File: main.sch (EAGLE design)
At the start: 9 parts, among them IC1 7805TV, IC3 LP298XS, U1 6SLX9TQG144

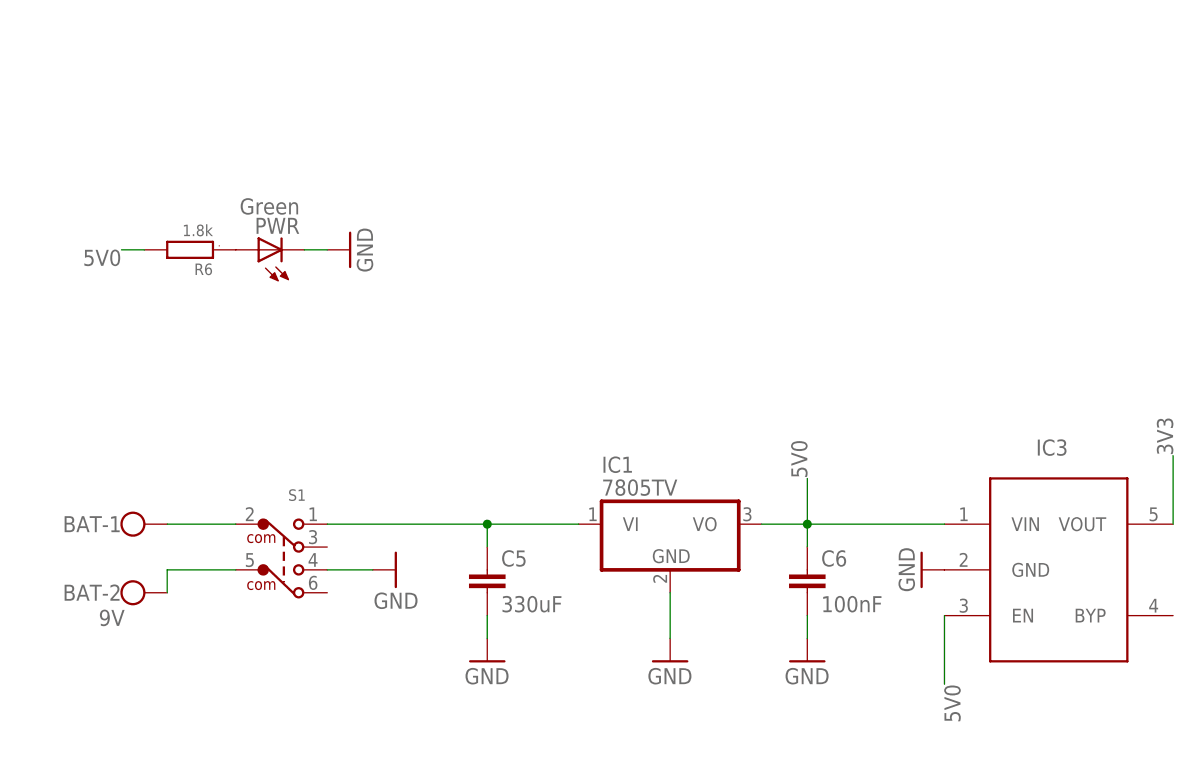
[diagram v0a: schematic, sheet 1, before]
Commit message: Replace voltage regulator to add 1V2 line
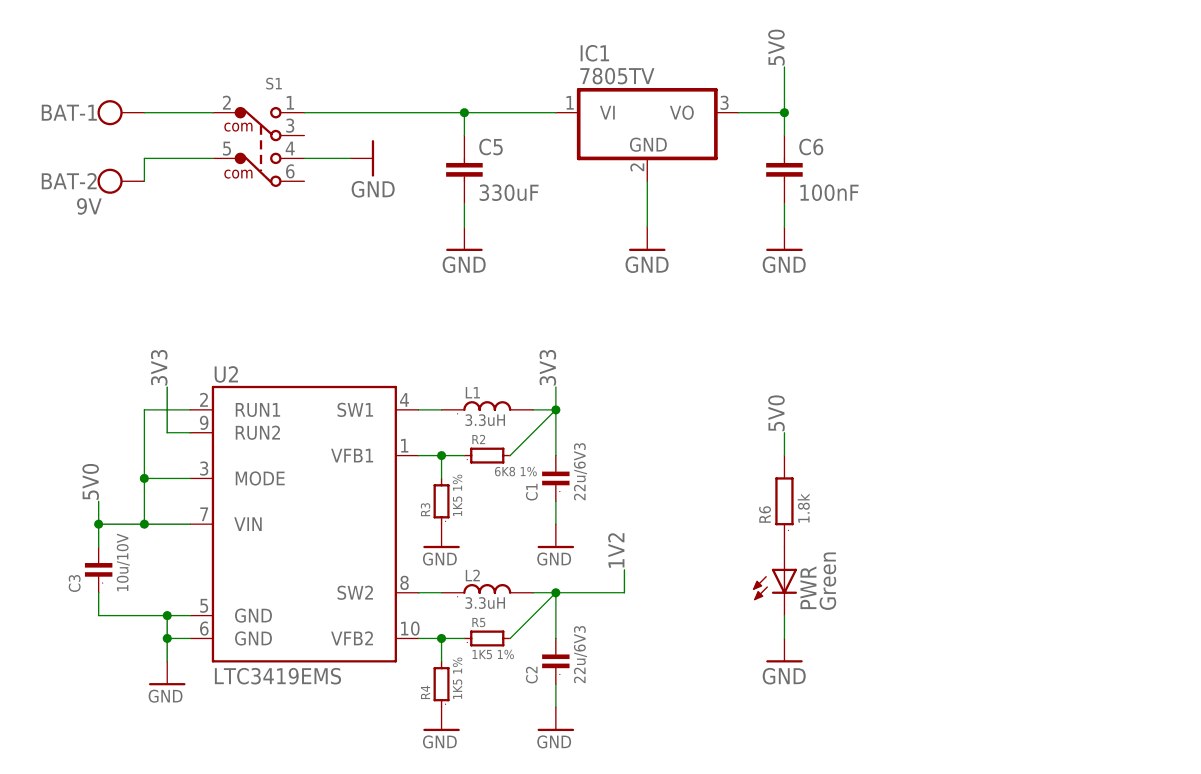
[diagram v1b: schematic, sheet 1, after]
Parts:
- removed IC3: LP298XS, adafruit:LP298XS
- added C1, C2: 22u/6V3, Bogdan_Commons:C0805
- added C3: 10u/10V, Bogdan_Commons:C0805
- added L1, L2: 3.3uH, Bogdan_Commons:L_VLS3015
- added R2: 6K8 1%, Bogdan_Commons:R-SMALL0603
- added R3, R4, R5: 1K5 1%, Bogdan_Commons:R-SMALL0603
- added U2: LTC3419EMS, Bogdan_Commons:LTC3419EMS
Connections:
- new net FB_1V2: R4.2, R5.1, U2.VFB2
- new net FB_3V3: R2.1, R3.2, U2.VFB1
- new net SW_1V2: L2.1, U2.SW2
- new net SW_3V3: L1.1, U2.SW1
- net 1V2: now also C2.2, L2.2, R5.2
- net 3V3: now also C1.2, L1.2, R2.2, U2.RUN2; no longer IC3.VOUT
- net 5V0: now also C3.2, U2.MODE, U2.RUN1, U2.VIN; no longer IC3.EN, IC3.VIN
- net GND: now also C1.1, C2.1, C3.1, R3.1, R4.1, U2.GND@5, U2.GND@6; no longer IC3.GND
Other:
- note added: "delays 1V2 start"
- moved on the sheet: BAT-1, BAT-2, C5, C6, IC1, PWR, R6, S1
